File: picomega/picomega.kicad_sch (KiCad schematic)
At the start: 27 parts, among them J5 PicoMega, Q4 BSS138, Q5 BSS138, Q6 BSS138, Q7 BSS138, SW1 SW_Push, U4 AMS1117-5.0 SOT-223

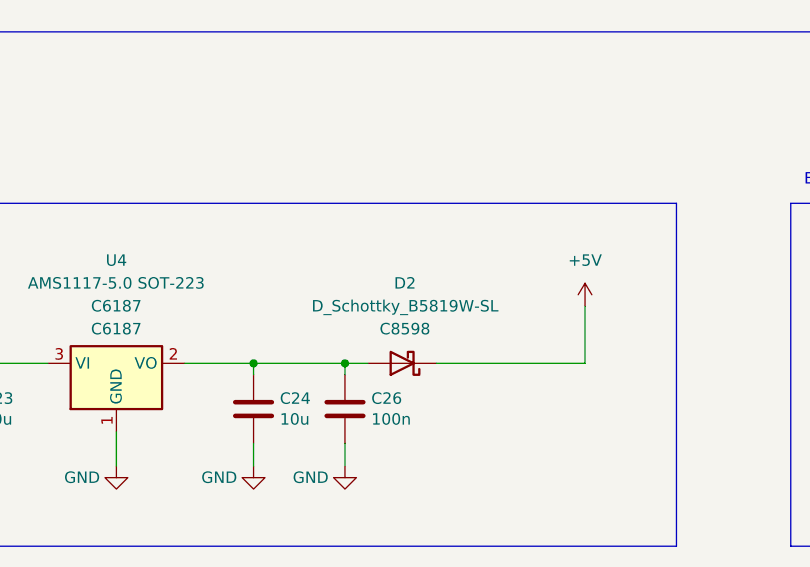
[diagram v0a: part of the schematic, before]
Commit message: update PicoMega to KiCad version 10
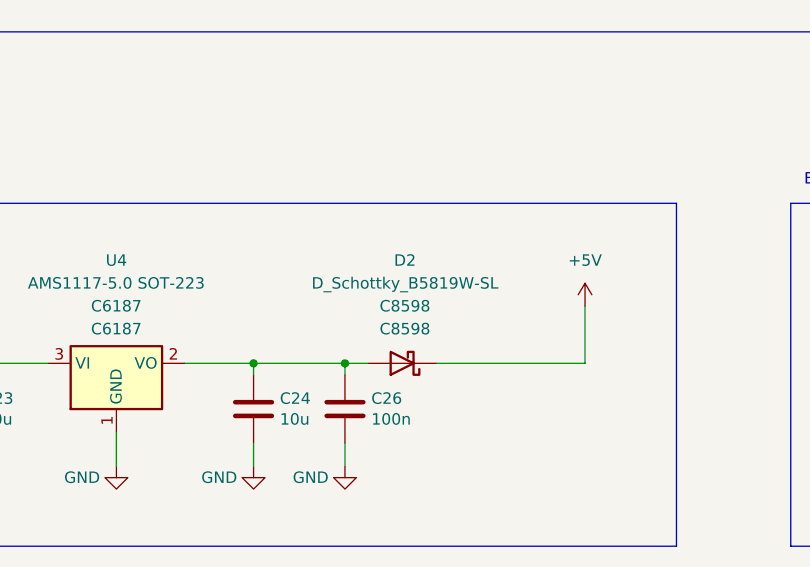
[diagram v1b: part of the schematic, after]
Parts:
- D2: symbol Own_Library:D_Schottky_B5819W-SL -> MobiFlight:D_Schottky_B5819W-SL

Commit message: update PicoMega acc new lib structure
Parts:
- J5: footprint MobiFlight:PicoMega -> Own_Library:PicoMega
- Q4, Q5, Q6, Q7: footprint PCM_JLCPCB:Q_SOT-23 -> Package_TO_SOT_SMD:SOT-23; symbol PCM_JLCPCB-Transistors:NMOS,BSS138 -> Transistor_FET:BSS138
- SW1: footprint MobiFlight:SW_Push_1P1T_NO_Vertical_Wuerth_434133025816 -> Own_Library:SW_Push_1P1T_NO_Vertical_Wuerth_434133025816
